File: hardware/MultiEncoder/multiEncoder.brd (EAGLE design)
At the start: 80 x 100 mm, 51 parts, among them J1 90325-0004, J2 90325-0004, U1 PCA9698DGG-518

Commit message: change to 8 knob per module, 64 knob max
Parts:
- removed MT10, MT11, MT12, MT13, MT14, MT15, MT16, MT9: PEC11R-4215F-S0024, PEC11R-4215F-S0024:XDCR_PEC11R-4215F-S0024
- removed R10, R11, R12, R13, R14, R15, R16, R17, R18, R19, R20, R21, R22, R23, R24, R25, R26, R27, R28, R29, R30, R31, R32, R7, R8, R9: 10K, rcl:R0805
- removed U1: PCA9698DGG-518, PCA9698DGG_518:SOP50P810X120-56N
- added J3, J4: 90325-0004, 90325-0004:MOLEX_90325-0004
- added U2: MCP23017T-E/SS, MCP23017T-E_SS:SOP65P780X200-28N
- R1, R3, R5: value 10K -> 1
- R2, R4, R6: value 10K -> 0
- moved J2 141.3 mm to (94.0, 40.0), turned to 270 degrees
- moved R5 100.3 mm to (17.0, 9.00), turned to 270 degrees
- moved R6 93.2 mm to (17.0, 4.00), turned to 270 degrees
- moved R2 92.6 mm to (42.0, 4.00), turned to 270 degrees
- moved R3 92.4 mm to (30.0, 9.00), turned to 270 degrees
- moved R1 92.4 mm to (42.0, 9.00), turned to 270 degrees
- moved J1 88.1 mm to (7.00, 40.0), turned to 270 degrees
- moved R4 85.5 mm to (30.0, 4.00), turned to 270 degrees
- moved MT8 40.0 mm to (87.5, 24.0)
- moved MT7 38.1 mm to (62.5, 24.0)
- moved MT6 36.8 mm to (37.5, 24.0)
- moved MT5 36.1 mm to (12.5, 24.0)
- moved MT4 28.1 mm to (87.5, 58.0)
- moved MT3 25.9 mm to (62.5, 58.0)
- moved MT2 23.9 mm to (37.5, 58.0)
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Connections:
- removed net A10: MT10.A, R20.1, U1.25
- removed net A11: MT11.A, R22.1, U1.31
- removed net A12: MT12.A, R24.1, U1.33
- removed net A13: MT13.A, R26.1, U1.36
- removed net A14: MT14.A, R28.1, U1.38
- removed net A15: MT15.A, R30.1, U1.41
- removed net A16: MT16.A, R32.1, U1.43
- removed net A9: MT9.A, R18.1, U1.22
- removed net B10: MT10.B, R19.1, U1.26
- removed net B11: MT11.B, R21.1, U1.32
- removed net B12: MT12.B, R23.1, U1.35
- removed net B13: MT13.B, R25.1, U1.37
- removed net B14: MT14.B, R27.1, U1.40
- removed net B15: MT15.B, R29.1, U1.42
- removed net B16: MT16.B, R31.1, U1.44
- removed net B9: MT9.B, R17.1, U1.24
- removed net VDD: U1.18, U1.46
- removed net VSS: U1.11, U1.23, U1.34, U1.39, U1.51, U1.6
- new net ADR0: R1.2, R2.1, U2.15
- new net ADR1: R3.2, R4.1, U2.16
- new net ADR2: R5.2, R6.1, U2.17
- net A1: now also U2.21; no longer R1.1, U1.3
- net A2: now also U2.23; no longer R4.1, U1.5
- net A3: now also U2.25; no longer R6.1, U1.8
- net A4: now also U2.27; no longer R8.1, U1.10
- net A5: now also U2.1; no longer R10.1, U1.13
- net A6: now also U2.3; no longer R12.1, U1.15
- net A7: now also U2.5; no longer U1.17
- net A7\: no longer R14.1
- net A8: now also U2.7; no longer R16.1, U1.20
- net B1: now also U2.22; no longer R2.1, U1.4
- net B2: now also U2.24; no longer R3.1, U1.7
- net B3: now also U2.26; no longer R5.1, U1.9
- net B4: now also U2.28; no longer R7.1, U1.12
- net B5: now also U2.2; no longer R9.1, U1.14
- net B6: now also U2.4; no longer R11.1, U1.16
- net B7: now also U2.6; no longer R13.1, U1.19
- net B8: now also U2.8; no longer R15.1, U1.21
- net GND: now also J3.2, J4.2, R2.2, R4.2, R6.2, U2.10; no longer MT10.COM, MT10.S1, MT10.S2, MT11.COM, MT11.S1, MT11.S2, MT12.COM, MT12.S1, MT12.S2, MT13.COM, MT13.S1, MT13.S2, MT14.COM, MT14.S1, MT14.S2, MT15.COM, MT15.S1, MT15.S2, MT16.COM, MT16.S1, MT16.S2, MT9.COM, MT9.S1, MT9.S2
- net SCL: now also J3.3, J4.3, U2.12
- net SDA: now also J3.4, J4.4, U2.13
- net VCC: now also J3.1, J4.1, R1.1, R3.1, R5.1, U2.18, U2.9; no longer R1.2, R10.2, R11.2, R12.2, R13.2, R14.2, R15.2, R16.2, R17.2, R18.2, R19.2, R2.2, R20.2, R21.2, R22.2, R23.2, R24.2, R25.2, R26.2, R27.2, R28.2, R29.2, R3.2, R30.2, R31.2, R32.2, R4.2, R5.2, R6.2, R7.2, R8.2, R9.2
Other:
- board size 80 x 100 mm -> 100 x 80 mm
- board text added: "A0"
- board text added: "A1"
- board text added: "A2"
- board text added: "ADRR = 0 1 0 0 A2 A1 A0"
- board text added: "SHORT ONLY ONE RESISTOR PER ADDR LINE"

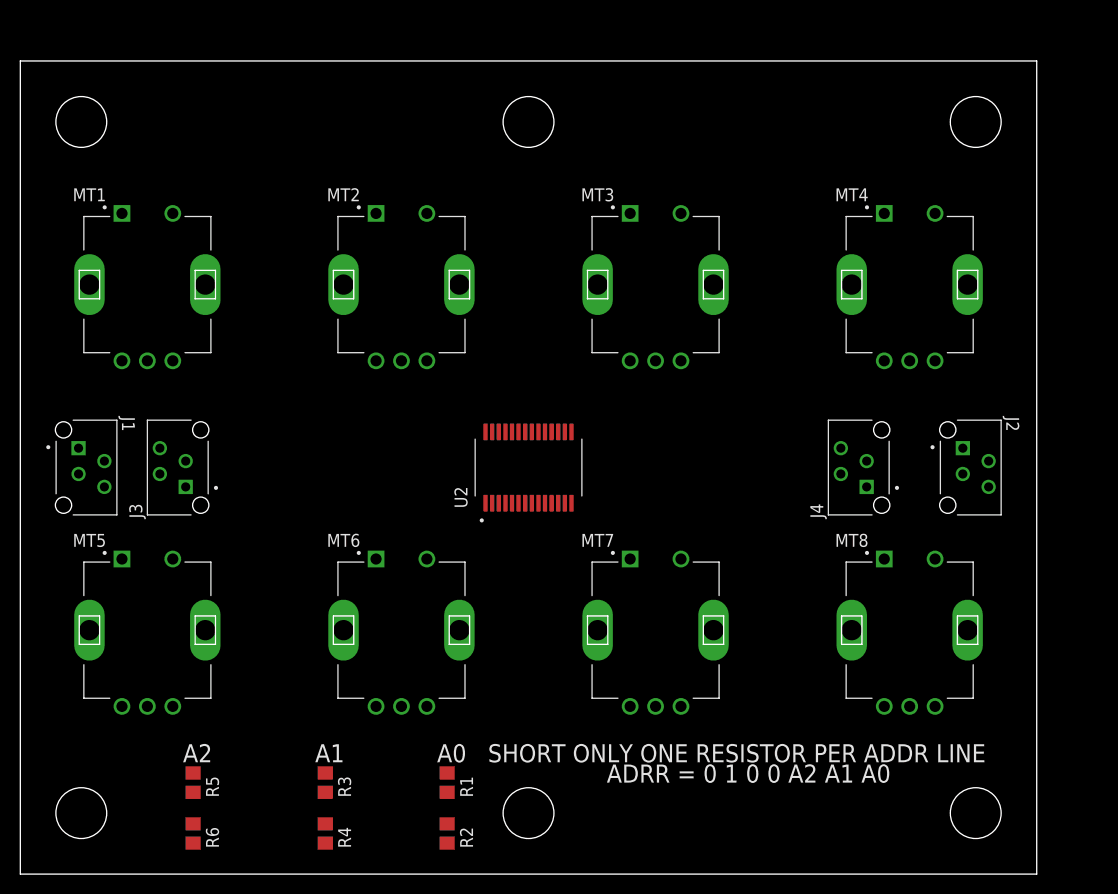
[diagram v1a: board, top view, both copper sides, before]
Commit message: Parts are placed, add ploygons and optional i2c line pullups
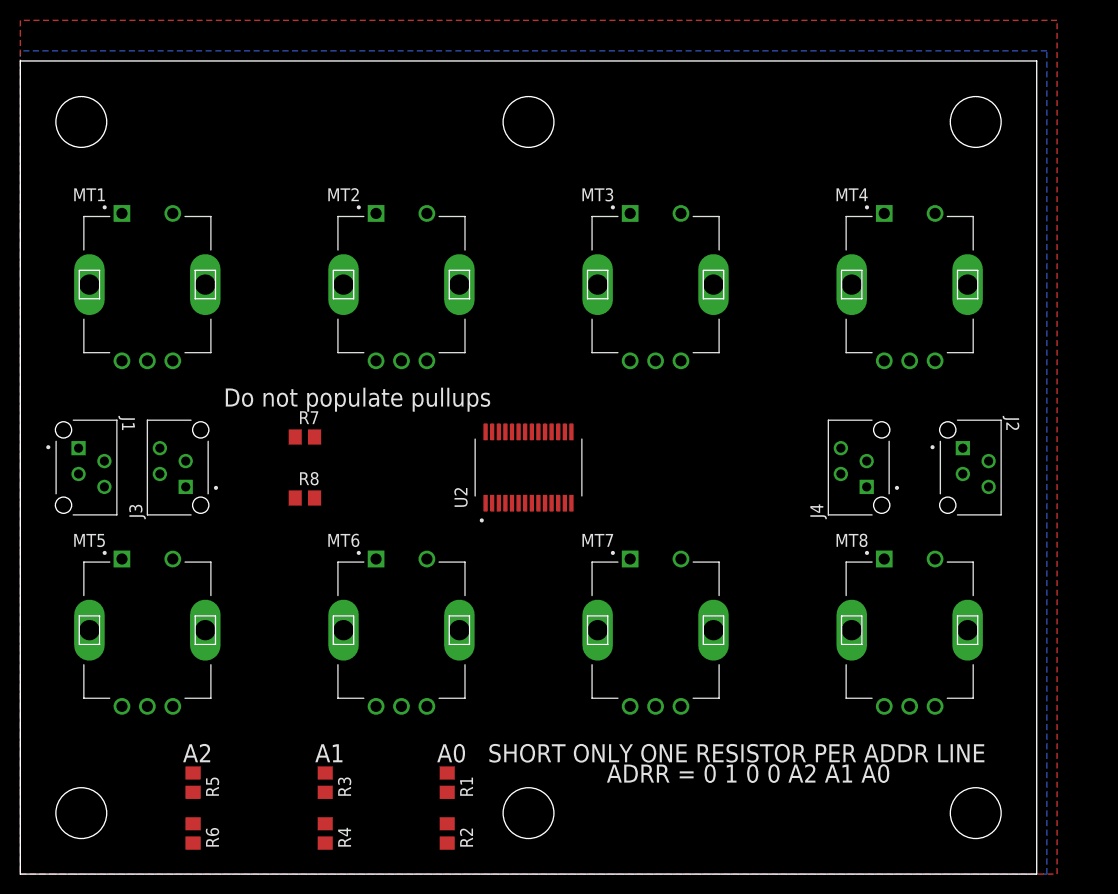
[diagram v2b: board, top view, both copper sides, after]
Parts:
- added R7, R8: 1K, rcl:R0805
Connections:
- net SCL: now also R7.2
- net SDA: now also R8.2
- net VCC: now also R7.1, R8.1
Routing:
- added copper zone on layer 16, net GND
- added copper zone on layer 1, net VCC
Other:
- board text added: "Do not populate pullups"
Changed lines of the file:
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@@
 <text x="29" y="11" size="1.778" layer="21">A1</text>
 <text x="41" y="11" size="1.778" layer="21">A0</text>
+<text x="20" y="46" size="1.778" layer="21">Do not populate pullups</text>
 </plain>
 <attributes>
@@
 <attribute name="VALUE" x="14.46" y="4.635" size="1.27" layer="27" rot="R270"/>
 </element>
+<element name="R7" library="rcl" library_urn="urn:adsk.eagle:library:334" package="R0805" package3d_urn="urn:adsk.eagle:package:23553/2" value="1K" x="28" y="43" smashed="yes">
+<attribute name="NAME" x="27.365" y="44.27" size="1.27" layer="25"/>
+<attribute name="POPULARITY" value="85" x="23" y="50" size="1.778" layer="27" display="off"/>
+<attribute name="SPICEPREFIX" value="R" x="23" y="50" size="1.778" layer="27" display="off"/>
+<attribute name="VALUE" x="27.365" y="40.46" size="1.27" layer="27"/>
+</element>
+<element name="R8" library="rcl" library_urn="urn:adsk.eagle:library:334" package="R0805" package3d_urn="urn:adsk.eagle:package:23553/2" value="1K" x="28" y="37" smashed="yes">
+<attribute name="NAME" x="27.365" y="38.27" size="1.27" layer="25"/>
+<attribute name="POPULARITY" value="85" x="28" y="37" size="1.778" layer="27" display="off"/>
+<attribute name="SPICEPREFIX" value="R" x="28" y="37" size="1.778" layer="27" display="off"/>
+<attribute name="VALUE" x="27.365" y="34.46" size="1.27" layer="27"/>
+</element>
 </elements>
 <signals>
@@
 <contactref element="R4" pad="2"/>
 <contactref element="R6" pad="2"/>
+<polygon width="0.1524" layer="16">
+<vertex x="101" y="0"/>
+<vertex x="101" y="81"/>
+<vertex x="0" y="81"/>
+<vertex x="0" y="0"/>
+<vertex x="0" y="0"/>
+<vertex x="3" y="0"/>
+<vertex x="5" y="0"/>
+</polygon>
 <wire x1="87.5" y1="50.5" x2="93.2" y2="58" width="0" layer="19" extent="1-1"/>
 <wire x1="81.8" y1="58" x2="87.5" y2="50.5" width="0" layer="19" extent="1-1"/>
@@
 <wire x1="12.5" y1="16.5" x2="18.2" y2="24" width="0" layer="19" extent="1-1"/>
 <wire x1="6.8" y1="24" x2="12.5" y2="16.5" width="0" layer="19" extent="1-1"/>
-<wire x1="42" y1="3.05" x2="12.5" y2="16.5" width="0" layer="19" extent="1-1"/>
+<wire x1="42" y1="3.05" x2="37.5" y2="16.5" width="0" layer="19" extent="1-1"/>
 <wire x1="30" y1="3.05" x2="42" y2="3.05" width="0" layer="19" extent="1-1"/>
 <wire x1="17" y1="3.05" x2="30" y2="3.05" width="0" layer="19" extent="1-1"/>
@@
 <contactref element="R5" pad="1"/>
 <contactref element="U2" pad="18"/>
+<contactref element="R7" pad="1"/>
+<contactref element="R8" pad="1"/>
+<polygon width="0.1524" layer="1">
+<vertex x="0" y="83"/>
+<vertex x="0" y="0"/>
+<vertex x="102" y="0"/>
+<vertex x="102" y="84"/>
+<vertex x="0" y="84"/>
+</polygon>
 <wire x1="83.27" y1="38.095" x2="92.73" y2="41.905" width="0" layer="19" extent="1-1"/>
 <wire x1="52.275" y1="43.505" x2="83.27" y2="38.095" width="0" layer="19" extent="1-1"/>
 <wire x1="50.975" y1="36.495" x2="52.275" y2="43.505" width="0" layer="19" extent="1-1"/>
-<wire x1="42" y1="9.95" x2="50.975" y2="36.495" width="0" layer="19" extent="1-1"/>
-<wire x1="30" y1="9.95" x2="42" y2="9.95" width="0" layer="19" extent="1-1"/>
+<wire x1="27.05" y1="37" x2="50.975" y2="36.495" width="0" layer="19" extent="1-1"/>
+<wire x1="27.05" y1="43" x2="27.05" y2="37" width="0" layer="19" extent="1-1"/>
+<wire x1="16.27" y1="38.095" x2="27.05" y2="37" width="0" layer="19" extent="1-1"/>
+<wire x1="5.73" y1="41.905" x2="16.27" y2="38.095" width="0" layer="19" extent="1-1"/>
+<wire x1="30" y1="9.95" x2="27.05" y2="37" width="0" layer="19" extent="1-1"/>
+<wire x1="42" y1="9.95" x2="30" y2="9.95" width="0" layer="19" extent="1-1"/>
 <wire x1="17" y1="9.95" x2="30" y2="9.95" width="0" layer="19" extent="1-1"/>
-<wire x1="16.27" y1="38.095" x2="17" y2="9.95" width="0" layer="19" extent="1-1"/>
-<wire x1="5.73" y1="41.905" x2="16.27" y2="38.095" width="0" layer="19" extent="1-1"/>
 </signal>
 <signal name="SCL">
@@
 <contactref element="J3" pad="3"/>
 <contactref element="J4" pad="3"/>
+<contactref element="R7" pad="2"/>
 <wire x1="83.27" y1="40.635" x2="92.73" y2="39.365" width="0" layer="19" extent="1-1"/>
 <wire x1="52.925" y1="36.495" x2="83.27" y2="40.635" width="0" layer="19" extent="1-1"/>
 <wire x1="16.27" y1="40.635" x2="52.925" y2="36.495" width="0" layer="19" extent="1-1"/>
 <wire x1="5.73" y1="39.365" x2="16.27" y2="40.635" width="0" layer="19" extent="1-1"/>
+<wire x1="28.95" y1="43" x2="5.73" y2="39.365" width="0" layer="19" extent="1-1"/>
 </signal>
 <signal name="SDA">
@@
 <contactref element="J3" pad="4"/>
 <contactref element="J4" pad="4"/>
+<contactref element="R8" pad="2"/>
 <wire x1="80.73" y1="41.905" x2="95.27" y2="38.095" width="0" layer="19" extent="1-1"/>
 <wire x1="53.575" y1="36.495" x2="80.73" y2="41.905" width="0" layer="19" extent="1-1"/>
 <wire x1="13.73" y1="41.905" x2="53.575" y2="36.495" width="0" layer="19" extent="1-1"/>
 <wire x1="8.27" y1="38.095" x2="13.73" y2="41.905" width="0" layer="19" extent="1-1"/>
+<wire x1="28.95" y1="37" x2="8.27" y2="38.095" width="0" layer="19" extent="1-1"/>
 </signal>
 <signal name="A2">

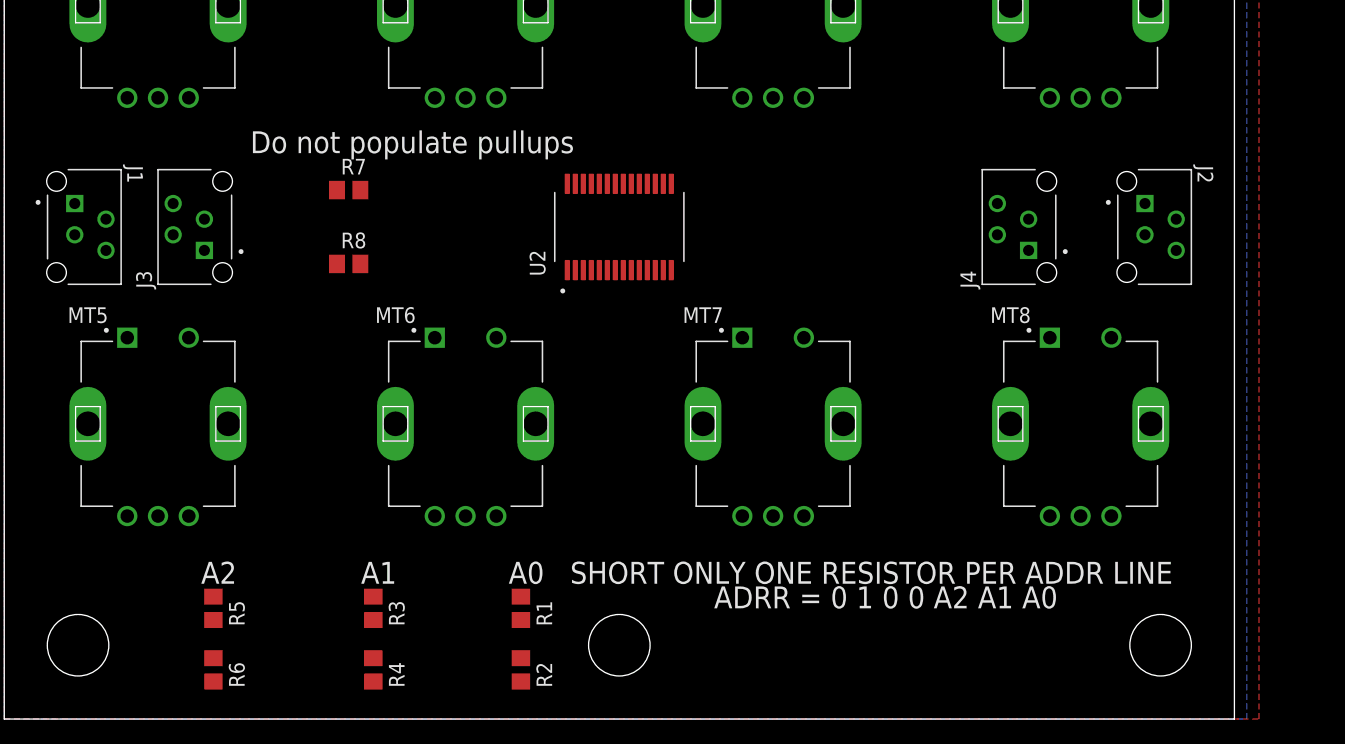
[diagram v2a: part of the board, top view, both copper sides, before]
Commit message: run autorouter on all signals beddides addr lines
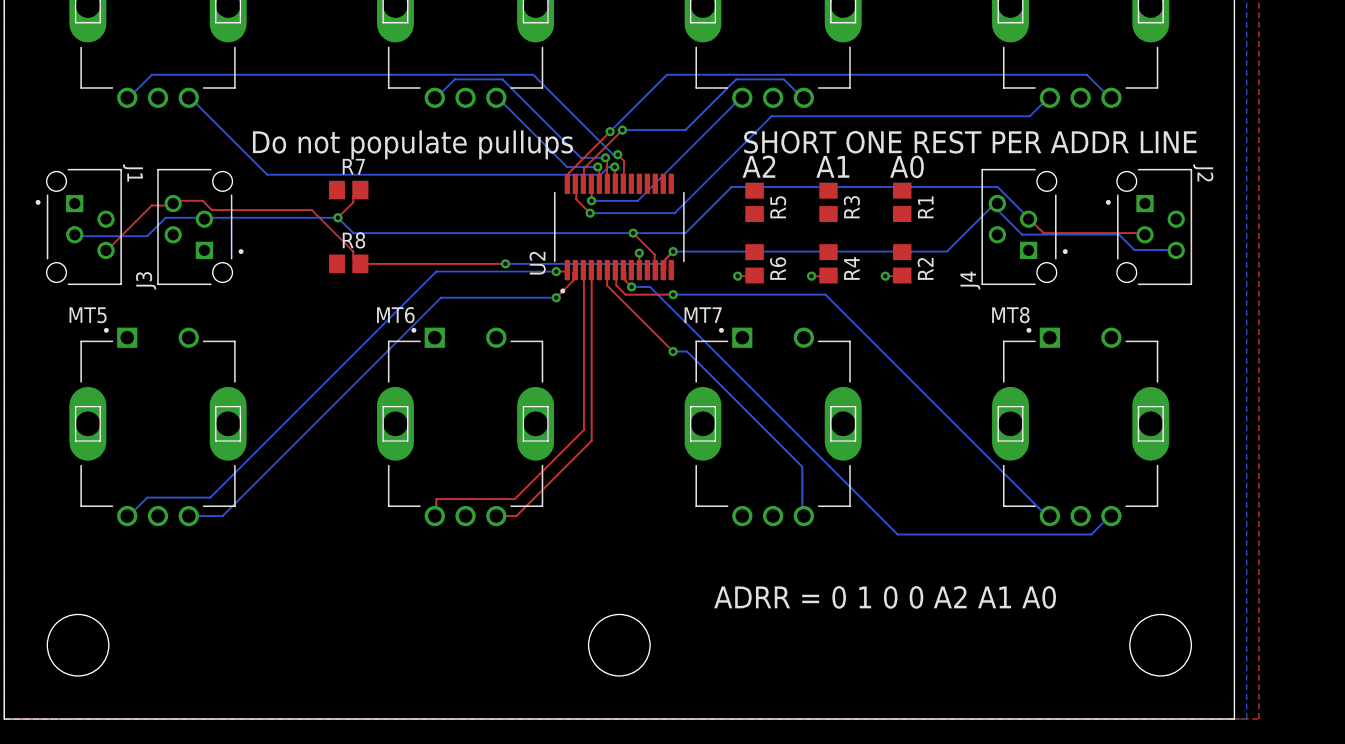
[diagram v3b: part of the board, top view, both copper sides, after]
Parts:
- moved R5 55.0 mm to (61.0, 42.0)
- moved R6 55.0 mm to (61.0, 37.0)
- moved R3 49.6 mm to (67.0, 42.0)
- moved R4 49.6 mm to (67.0, 37.0)
- moved R1 45.3 mm to (73.0, 42.0)
- moved R2 45.3 mm to (73.0, 37.0)
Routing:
- net SCL: track 0.00 -> 98.5 mm, vias 0 -> 2
- net SDA: track 0.00 -> 97.5 mm, vias 0 -> 2
- net B8: track 0.00 -> 49.6 mm, vias 0 -> 1
- net B4: track 0.00 -> 49.1 mm, vias 0 -> 1
- net A1: track 0.00 -> 45.9 mm, vias 0 -> 1
- net A8: track 0.00 -> 44.3 mm, vias 0 -> 1
- net A4: track 0.00 -> 44.2 mm, vias 0 -> 1
- net A5: track 0.00 -> 44.1 mm, vias 0 -> 1
- net B5: track 0.00 -> 40.1 mm, vias 0 -> 1
- net B1: track 0.00 -> 38.9 mm, vias 0 -> 1
- net A6: track 0.00 -> 28.8 mm
- net B7: track 0.00 -> 27.3 mm, vias 0 -> 1
- net B6: track 0.00 -> 24.2 mm
- net B3: track 0.00 -> 22.8 mm, vias 0 -> 1
- net A2: track 0.00 -> 19.3 mm, vias 0 -> 1
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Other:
- board text added: "SHORT ONE REST PER ADDR LINE"
- board text removed: "SHORT ONLY ONE RESISTOR PER ADDR LINE"
